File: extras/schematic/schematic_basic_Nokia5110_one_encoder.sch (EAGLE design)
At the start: 25 parts, among them U1 SI4735-D60-GU

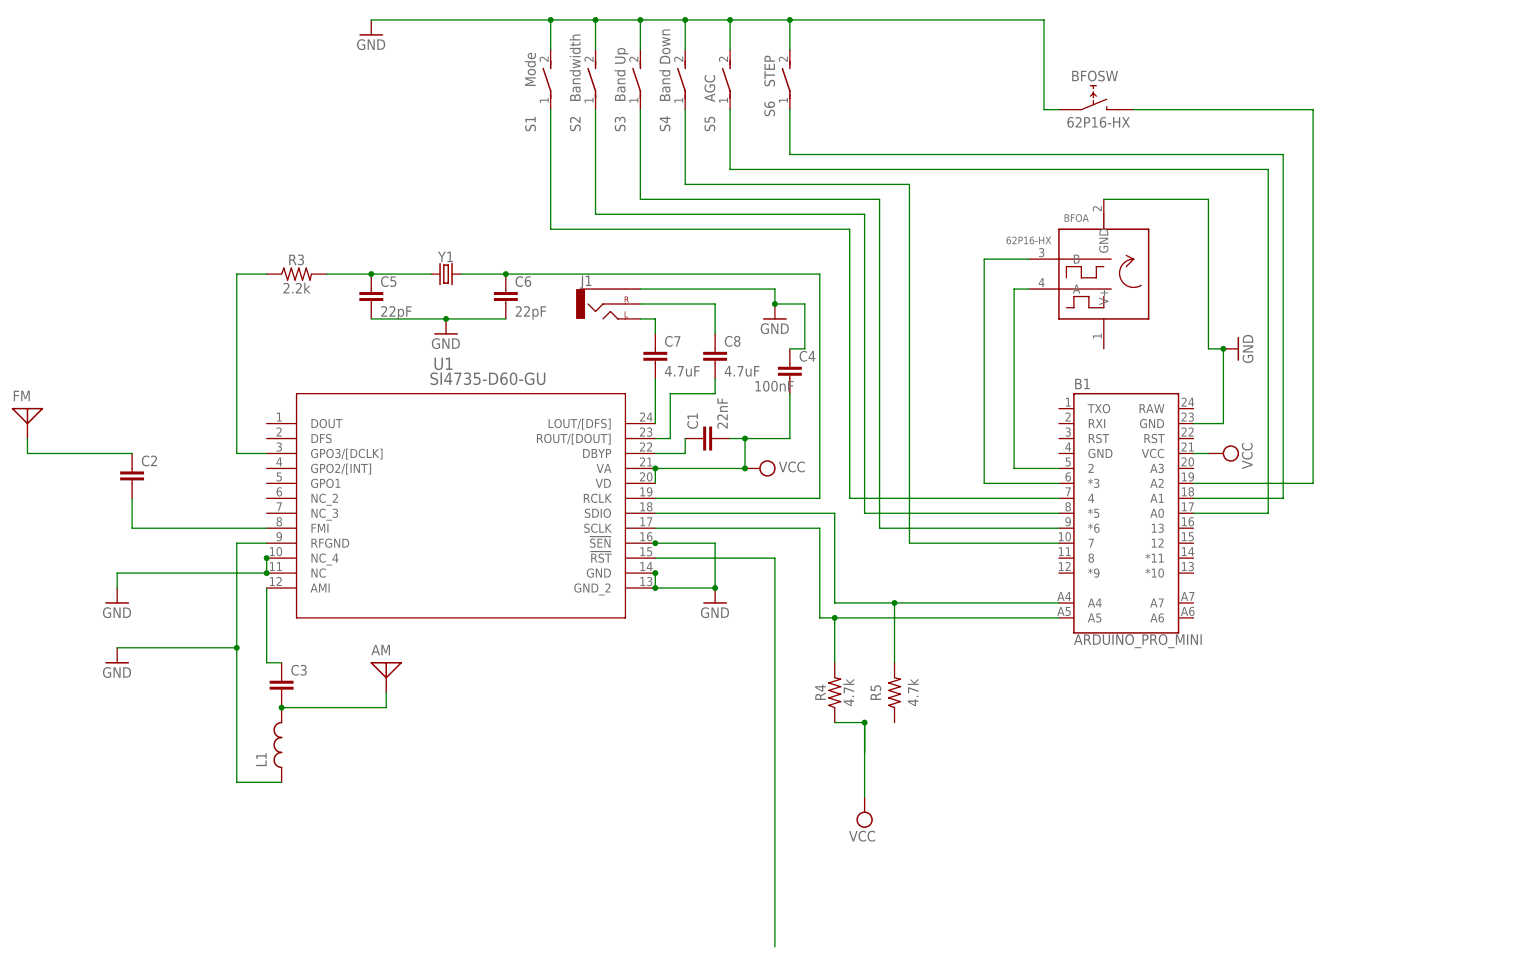
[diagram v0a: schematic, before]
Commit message: SI473X Arduino Library
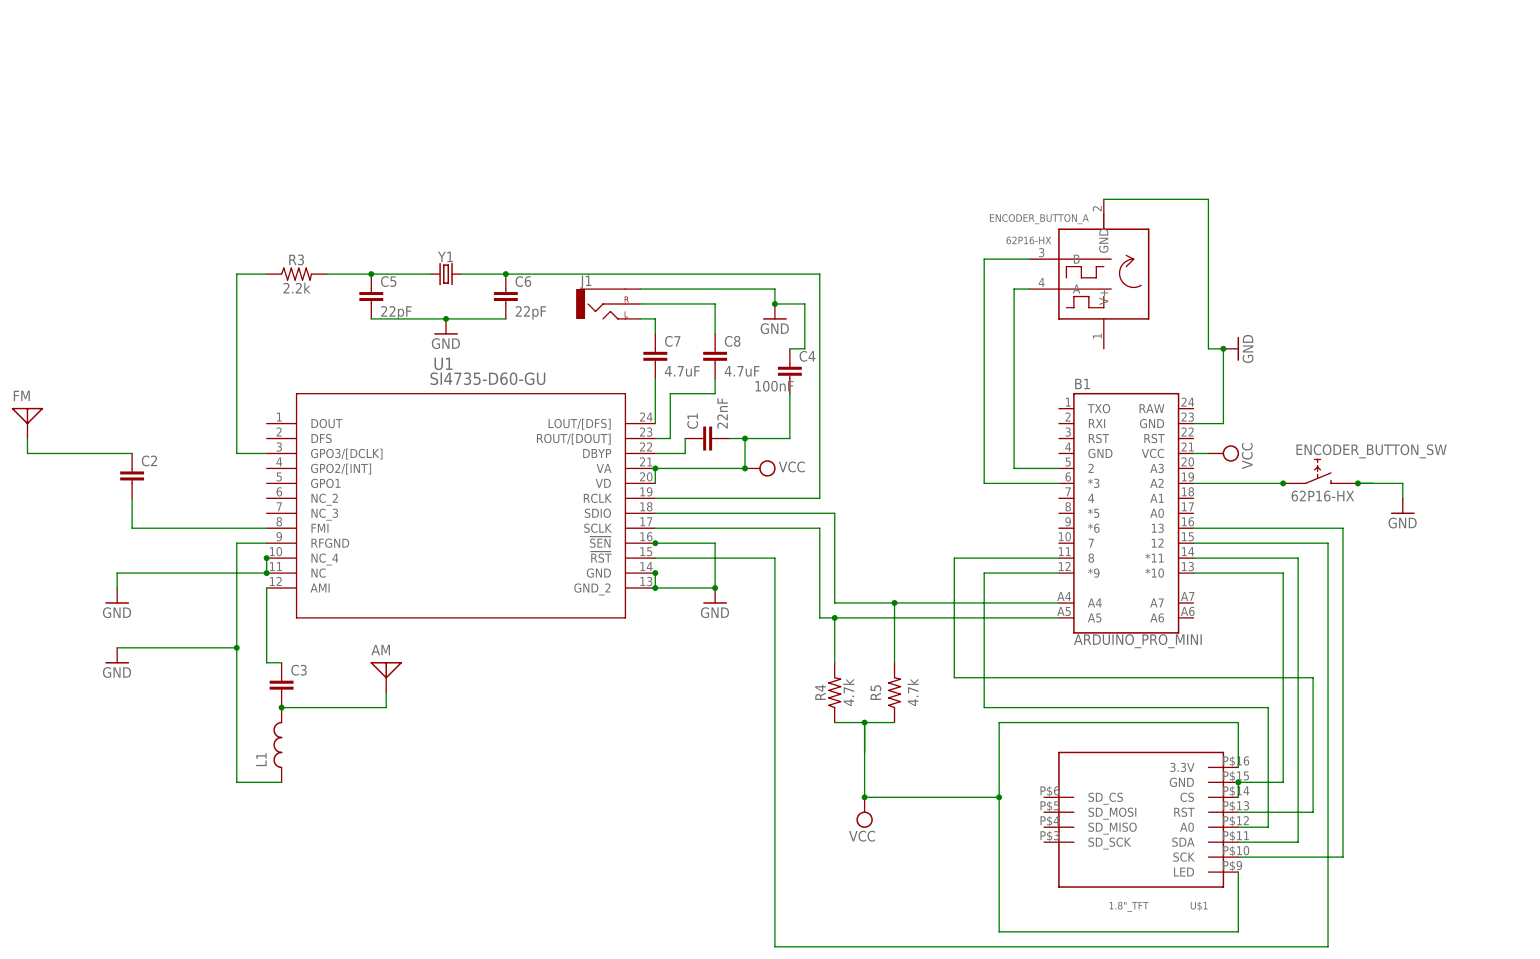
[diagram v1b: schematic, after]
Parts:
- removed S1: Mode, switch-dil:DS01E
- removed S2: Bandwidth, switch-dil:DS01E
- removed S3: Band Up, switch-dil:DS01E
- removed S4: Band Down, switch-dil:DS01E
- removed S5: AGC, switch-dil:DS01E
- removed S6: STEP, switch-dil:DS01E
- added U$1: 1.8"_TFT, tft_1_8_1_44_oled_0_96:1.8"_TFT
- renumbered BFO to ENCODER_BUTTON_
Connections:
- removed net N$18: B1.*5, S2.1
- removed net N$19: B1.*6, S3.1
- removed net N$20: B1.7, S4.1
- removed net N$21: B1.A0, S5.1
- removed net N$22: B1.A1, S6.1
- removed net N$28: B1.A2, ENCODER_BUTTON_SW.E
- new net N$23: B1.*10, U$1.CS, U$1.GND
- new net N$24: B1.13, U$1.SCK
- new net N$25: B1.8, U$1.RST
- new net N$26: B1.*11, U$1.SDA
- new net N$27: B1.*9, U$1.A0
- net GND: now also ENCODER_BUTTON_SW.E; no longer ENCODER_BUTTON_SW.D, S1.2, S2.2, S3.2, S4.2, S5.2, S6.2
- net N$1: now also B1.12
- net N$17: now also B1.A2, ENCODER_BUTTON_SW.D; no longer B1.4, S1.1
- net VCC: now also R5.1, U$1.3.3V, U$1.LED

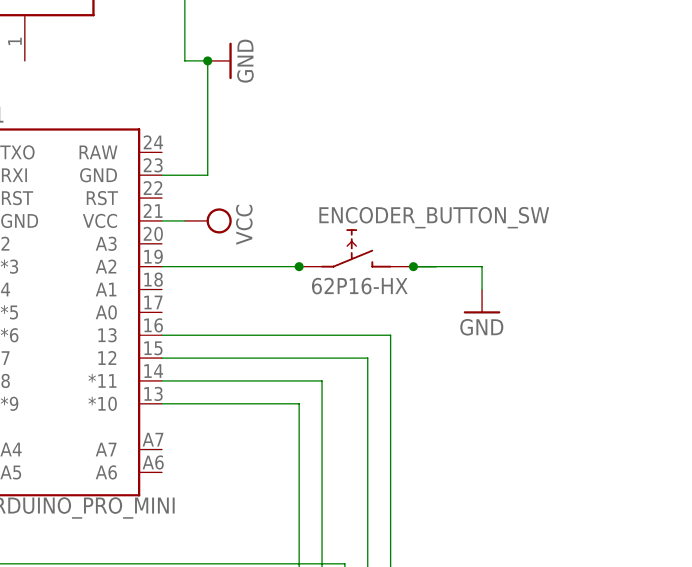
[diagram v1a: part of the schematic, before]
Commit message: SI473X Arduino Library
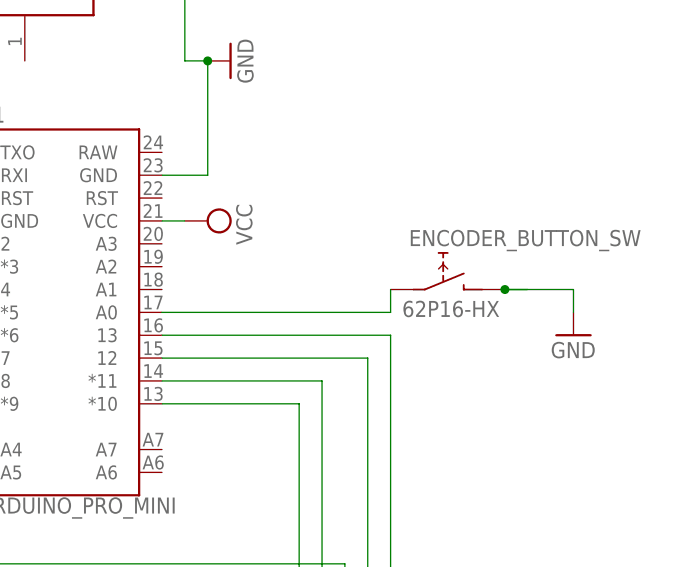
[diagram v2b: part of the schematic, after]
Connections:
- net N$17: now also B1.A0; no longer B1.A2
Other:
- moved on the sheet: ENCODER_BUTTON_SW
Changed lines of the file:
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@@
 <attribute name="VALUE" x="13.97" y="199.39" size="1.27" layer="96" rot="R180"/>
 </instance>
-<instance part="ENCODER_BUTTON_" gate="SW" x="58.42" y="160.02" smashed="yes">
-<attribute name="NAME" x="55.372" y="162.306" size="1.778" layer="95"/>
-<attribute name="VALUE" x="54.61" y="154.432" size="1.778" layer="96"/>
-</instance>
-<instance part="GND8" gate="1" x="73.66" y="152.4" smashed="yes">
-<attribute name="VALUE" x="71.12" y="149.86" size="1.778" layer="96"/>
+<instance part="ENCODER_BUTTON_" gate="SW" x="68.58" y="157.48" smashed="yes">
+<attribute name="NAME" x="65.532" y="159.766" size="1.778" layer="95"/>
+<attribute name="VALUE" x="64.77" y="151.892" size="1.778" layer="96"/>
+</instance>
+<instance part="GND8" gate="1" x="83.82" y="149.86" smashed="yes">
+<attribute name="VALUE" x="81.28" y="147.32" size="1.778" layer="96"/>
 </instance>
 <instance part="SUPPLY4" gate="G$1" x="-17.78" y="101.6" smashed="yes" rot="R180">
@@
 <segment>
 <pinref part="ENCODER_BUTTON_" gate="SW" pin="E"/>
-<wire x1="68.58" y1="157.48" x2="66.04" y2="157.48" width="0.1524" layer="91"/>
+<wire x1="78.74" y1="154.94" x2="76.2" y2="154.94" width="0.1524" layer="91"/>
 <pinref part="GND8" gate="1" pin="GND"/>
-<wire x1="73.66" y1="154.94" x2="73.66" y2="157.48" width="0.1524" layer="91"/>
-<wire x1="73.66" y1="157.48" x2="66.04" y2="157.48" width="0.1524" layer="91"/>
-<junction x="66.04" y="157.48"/>
+<wire x1="83.82" y1="152.4" x2="83.82" y2="154.94" width="0.1524" layer="91"/>
+<wire x1="83.82" y1="154.94" x2="76.2" y2="154.94" width="0.1524" layer="91"/>
+<junction x="76.2" y="154.94"/>
 </segment>
 </net>
@@
 <net name="N$17" class="0">
 <segment>
-<pinref part="B1" gate="G$1" pin="A2"/>
-<wire x1="38.1" y1="157.48" x2="53.34" y2="157.48" width="0.1524" layer="91"/>
 <pinref part="ENCODER_BUTTON_" gate="SW" pin="D"/>
-<junction x="53.34" y="157.48"/>
-</segment>
-</net>
+<wire x1="63.5" y1="154.94" x2="63.5" y2="152.4" width="0.1524" layer="91"/>
+<pinref part="B1" gate="G$1" pin="A0"/>
+<wire x1="63.5" y1="152.4" x2="38.1" y2="152.4" width="0.1524" layer="91"/>
+</segment>
+</net>
